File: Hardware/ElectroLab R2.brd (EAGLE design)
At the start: 175 x 100 mm, 226 parts, among them IC1 LM2902DT, IC10 CD4511BNSR, IC11 PAM8403, IC2 LM2902DT, IC3 SN74LV08ADR, IC4 SN74LV32ADR, IC5 SN74LV04ADR, IC6 4027D, IC7 4027D, IC8 NE555D, IC9 AT42QT1012, U1 USB, U2 USB-B

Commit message: Analogic accelerometer ADXL337 Layout in BRD
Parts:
- removed IR: CNY70, cny70:4
- added ACC: ADXL337, SpaceDIY_IC:LFCSP-3X3
- added C29, C30, C31: 10nF, SpaceDIY_passive_components:0603
- added C32: 100nF, SpaceDIY_passive_components:0603
- added C33, C34: 10uF, SpaceDIY_passive_components:0603
- added IC12: LM2902DT, Texas Instruments_By_element14_Batch_1:SOIC127P600X175-14N
- added R61, R63, R65: 1k, SpaceDIY_passive_components:0603
- added R62, R64, R66: 2k, SpaceDIY_passive_components:0603
- added U4: MIC5205, SparkFun:SOT23-5
- PH35: device pinhead:1X04 -> pinhead:1X03
- moved PH35 0.52 mm to (125.1, 46.7)
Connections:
- removed net A: IR.A, PH35.1
- removed net C: IR.C, PH35.3
- removed net E: IR.E, PH35.4
- removed net K: IR.K, PH35.2
- new net 3.3V: ACC.14, ACC.15, C32.1, C33.1, U4.5
- new net X: IC12.1, PH35.3, R61.1
- new net X+: ACC.5, C29.1, IC12.3
- new net X-: IC12.2, R61.2, R62.1
- new net Y: IC12.7, PH35.2, R63.1
- new net Y+: ACC.4, C30.1, IC12.5
- new net Y-: IC12.6, R63.2, R64.1
- new net Z: IC12.8, PH35.1, R65.1
- new net Z+: ACC.16, C31.1, IC12.10
- new net Z-: IC12.9, R65.2, R66.1
- net GND: now also ACC.6, ACC.7, C29.2, C30.2, C31.2, C32.2, C33.2, C34.2, IC12.11, R62.2, R64.2, R66.2, U4.2
- net VCC: now also C34.1, IC12.4, U4.1, U4.3
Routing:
- net VCC: track 395.1 -> 443.1 mm, vias 10 -> 12
- net Z: track 0.00 -> 28.8 mm, vias 0 -> 1
- net 3.3V: track 0.00 -> 22.1 mm, vias 0 -> 1
- net E: track 19.9 -> 0.00 mm
- net X+: track 0.00 -> 18.6 mm, vias 0 -> 1
- net X: track 0.00 -> 15.6 mm, vias 0 -> 1
- net Z-: track 0.00 -> 14.3 mm
- net Y: track 0.00 -> 13.5 mm
- net X-: track 0.00 -> 13.2 mm, vias 0 -> 2
- net C: track 12.5 -> 0.00 mm
- net Z+: track 0.00 -> 11.9 mm, vias 0 -> 1
- net Y+: track 0.00 -> 9.66 mm, vias 0 -> 1
- net K: track 8.81 -> 0.00 mm
- net A: track 8.78 -> 0.00 mm
- net Y-: track 0.00 -> 8.46 mm
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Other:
- board text added: "X"
- board text added: "Y"
- board text added: "Z"
- board text removed: "E"
- board text removed: "IR1"
- board text removed: "IR2"
- board text removed: "IR3"
- board text removed: "IR4"

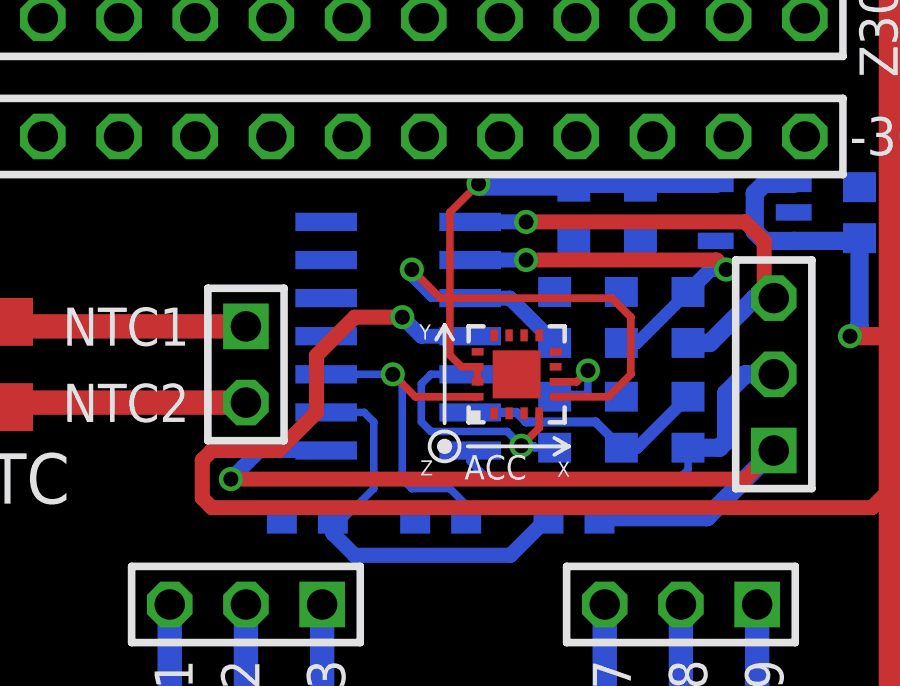
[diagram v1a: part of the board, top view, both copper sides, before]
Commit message: Minor update of ADXL337 layout
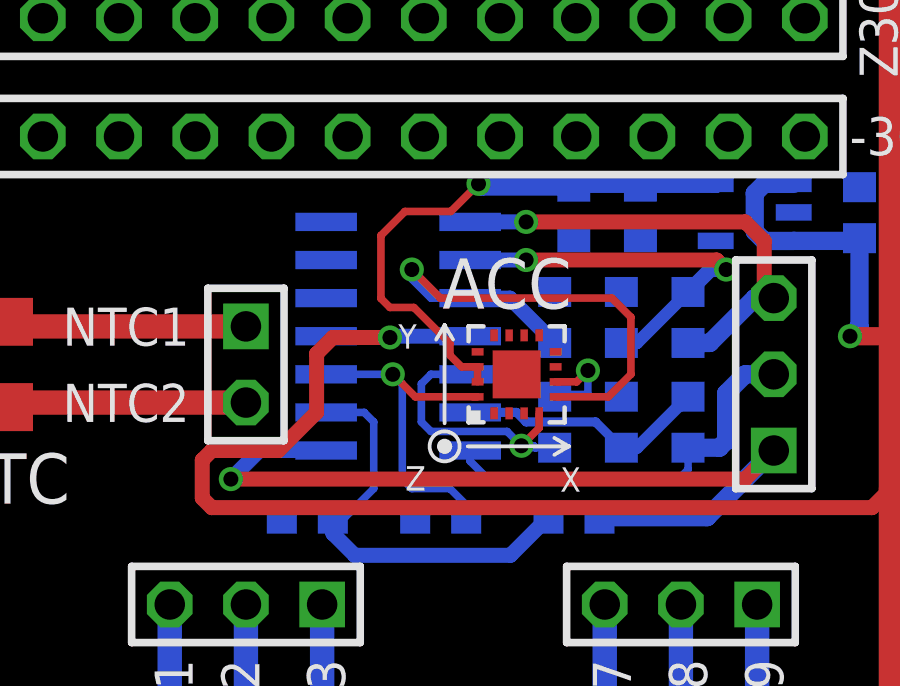
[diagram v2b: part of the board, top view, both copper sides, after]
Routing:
- net 3.3V: track 22.1 -> 25.4 mm
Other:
- board text added: "ACC"
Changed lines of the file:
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@@
 <setting verticaltext="up"/>
 </settings>
-<grid distance="0.001" unitdist="mm" unit="mm" style="lines" multiple="1" display="yes" altdistance="0.025" altunitdist="inch" altunit="inch"/>
+<grid distance="0.1" unitdist="mm" unit="mm" style="lines" multiple="1" display="yes" altdistance="0.025" altunitdist="inch" altunit="inch"/>
 <layers>
 <layer number="1" name="Top" color="4" fill="1" visible="yes" active="yes"/>
@@
 <text x="128.5875" y="61.2775" size="1.27" layer="112" rot="R90" align="center">Y30</text>
 <text x="128.5875" y="58.1025" size="1.27" layer="112" rot="R90" align="center">Z30</text>
+<text x="116.2" y="49.7" size="1.6764" layer="25" align="center">ACC</text>
 </plain>
 <attributes>
@@
 <via x="127.635" y="47.9425" extent="1-16" drill="0.5"/>
 <wire x1="127.635" y1="47.9425" x2="129" y2="47.9425" width="0.6096" layer="1"/>
-<wire x1="114.9731" y1="47.9425" x2="113.3475" y2="47.9425" width="0.5" layer="16"/>
-<wire x1="113.3475" y1="47.9425" x2="112.7125" y2="48.5775" width="0.5" layer="16"/>
-<via x="112.7125" y="48.5775" extent="1-16" drill="0.5"/>
-<wire x1="112.7125" y1="48.5775" x2="111.125" y2="48.5775" width="0.5" layer="1"/>
-<wire x1="111.125" y1="48.5775" x2="109.855" y2="47.3075" width="0.5" layer="1"/>
-<wire x1="109.855" y1="47.3075" x2="109.855" y2="45.4025" width="0.5" layer="1"/>
+<wire x1="109.855" y1="47.355" x2="109.855" y2="45.4025" width="0.5" layer="1"/>
 <wire x1="109.855" y1="45.4025" x2="108.585" y2="44.1325" width="0.5" layer="1"/>
 <wire x1="108.585" y1="44.1325" x2="106.3625" y2="44.1325" width="0.5" layer="1"/>
@@
 <wire x1="106.3625" y1="42.2275" x2="128.365" y2="42.2275" width="0.5" layer="1"/>
 <wire x1="128.365" y1="42.2275" x2="129" y2="42.8625" width="0.5" layer="1"/>
+<wire x1="109.855" y1="47.355" x2="110.4" y2="47.9" width="0.5" layer="1"/>
+<wire x1="110.4" y1="47.9" x2="111.8" y2="47.9" width="0.5" layer="1"/>
+<wire x1="114.9731" y1="47.9425" x2="112.3425" y2="47.9425" width="0.5" layer="16"/>
+<wire x1="112.3425" y1="47.9425" x2="112.3" y2="47.9" width="0.5" layer="16"/>
+<via x="112.3" y="47.9" extent="1-16" drill="0.5"/>
+<wire x1="112.3" y1="47.9" x2="111.8" y2="47.9" width="0.5" layer="1"/>
 </signal>
 <signal name="VEXT">
@@
 <wire x1="115.2225" y1="46.9215" x2="114.685" y2="46.9225" width="0.254" layer="1"/>
 <wire x1="114.685" y1="46.9225" x2="114.3" y2="47.3075" width="0.254" layer="1"/>
-<wire x1="114.3" y1="47.3075" x2="114.3" y2="52.07" width="0.254" layer="1"/>
-<wire x1="114.3" y1="52.07" x2="115.2525" y2="53.0225" width="0.254" layer="1"/>
 <via x="115.2525" y="53.0225" extent="1-16" drill="0.5"/>
 <wire x1="115.2525" y1="53.0225" x2="118.335" y2="53.0225" width="0.254" layer="16"/>
@@
 <wire x1="120.9675" y1="53.0225" x2="123.1574" y2="53.0225" width="0.6096" layer="16"/>
 <wire x1="123.1574" y1="53.0225" x2="123.1599" y2="53.02" width="0.6096" layer="16"/>
+<wire x1="114.3" y1="47.3075" x2="114.3" y2="47.7" width="0.254" layer="1"/>
+<wire x1="114.3" y1="47.7" x2="113.1" y2="48.9" width="0.254" layer="1"/>
+<wire x1="113.1" y1="48.9" x2="112.3" y2="48.9" width="0.254" layer="1"/>
+<wire x1="112.3" y1="48.9" x2="112" y2="49.2" width="0.254" layer="1"/>
+<wire x1="112" y1="49.2" x2="112" y2="51.3" width="0.254" layer="1"/>
+<wire x1="112" y1="51.3" x2="112.8" y2="52.1" width="0.254" layer="1"/>
+<wire x1="112.8" y1="52.1" x2="114.33" y2="52.1" width="0.254" layer="1"/>
+<wire x1="114.33" y1="52.1" x2="115.2525" y2="53.0225" width="0.254" layer="1"/>
 </signal>
 <signal name="X">

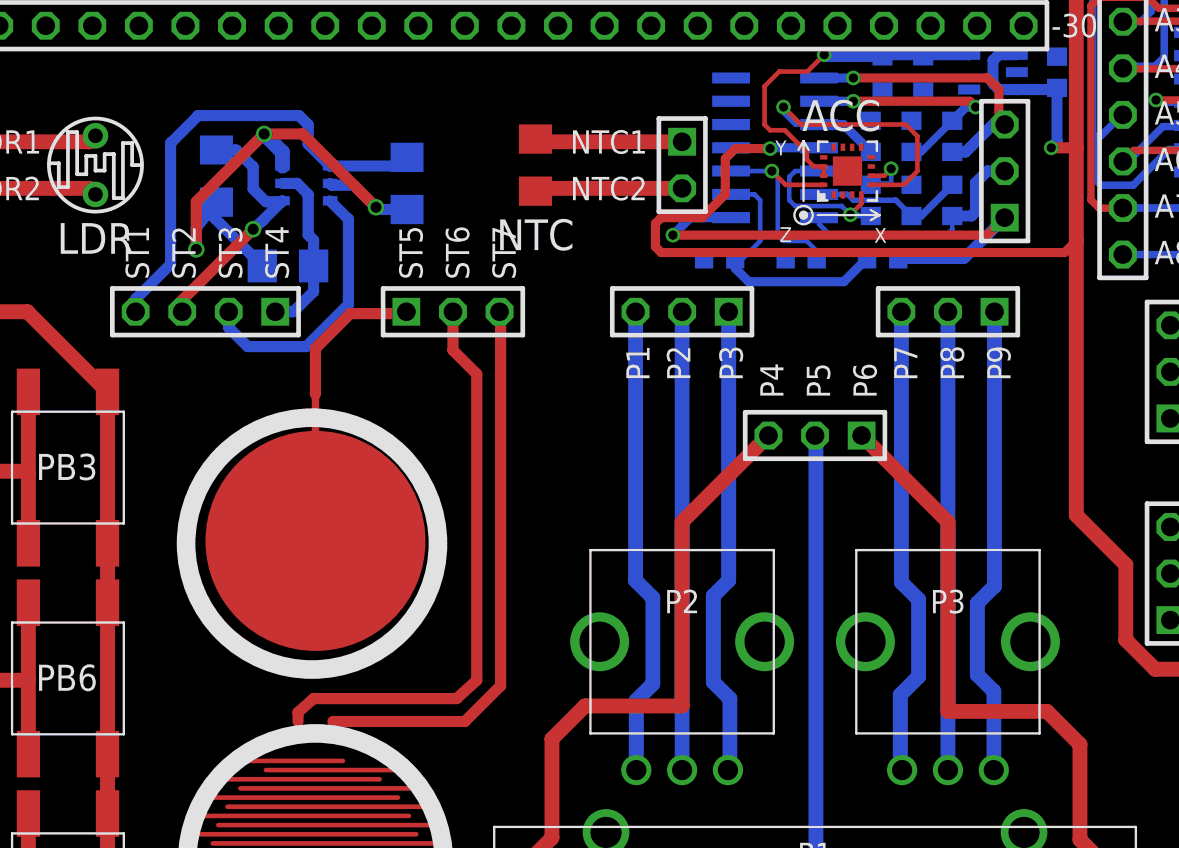
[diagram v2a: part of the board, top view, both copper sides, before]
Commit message: Modified capacitive tactile sensor. Simplified design.
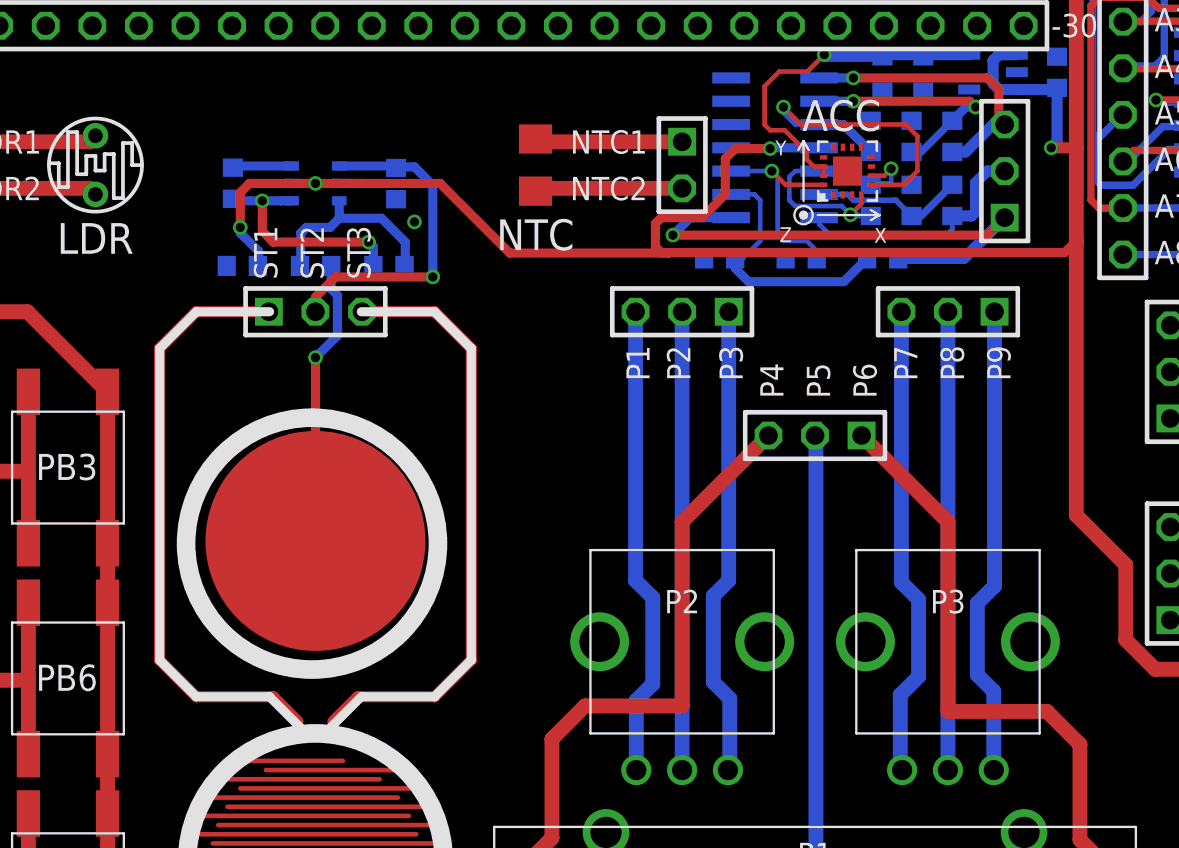
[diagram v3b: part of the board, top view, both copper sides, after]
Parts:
- removed PH34: (no value), pinhead:1X04
- added C28: 10nF, SpaceDIY_passive_components:0603
- added R67: 10k, SpaceDIY_passive_components:0603
- C22: device resistor:C1206 -> SpaceDIY_passive_components:0603
- R39, R40: device resistor:R1206 -> SpaceDIY_passive_components:0603
- moved PH21 7.50 mm to (87.5, 39.0)
- moved C22 2.50 mm to (83.5, 41.5)
- moved R40 0.98 mm to (83.0, 46.0), turned to 270 degrees
- moved R39 0.60 mm to (91.9, 46.0)
- moved IC9 0.50 mm to (87.5, 46.0)
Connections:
- removed net N$252: PH21.2, U$16.0
- removed net N$253: PH21.1, U$15.0
- removed net VCC01: C22.1, IC9.5, PH34.1
- new net N$125: PH21.1, U$16.0
- new net SENSE: R67.1, U$15.0
- net OUT01: now also PH21.2; no longer PH34.4
- net SNS: now also C28.2; no longer PH34.3
- net SNSK: now also C28.1, R67.2; no longer PH34.2
- net VCC: now also C22.1, IC9.5
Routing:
- net N$125: track 0.00 -> 32.7 mm
- net N$252: track 31.6 -> 0.00 mm
- net VCC: track 442.6 -> 473.5 mm, vias 12 -> 14
- net GND: track 92.8 -> 67.4 mm, vias 19 -> 17
- net SENSE: track 0.00 -> 9.74 mm, vias 0 -> 1
- net VCC01: track 9.62 -> 0.00 mm
- net N$253: track 8.29 -> 0.00 mm
- net OUT01: track 25.5 -> 18.2 mm, vias 0 -> 1
- net SNSK: track 14.8 -> 10.7 mm
- net N$126: track 30.4 -> 32.7 mm
- net SNS: track 13.8 -> 12.4 mm, vias 1 -> 2
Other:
- board text removed: "SNS"
- board text removed: "SNSK"
- board text removed: "ST4"
- board text removed: "ST5"
- board text removed: "ST6"
- board text removed: "ST7"
- board text removed: "VCC"

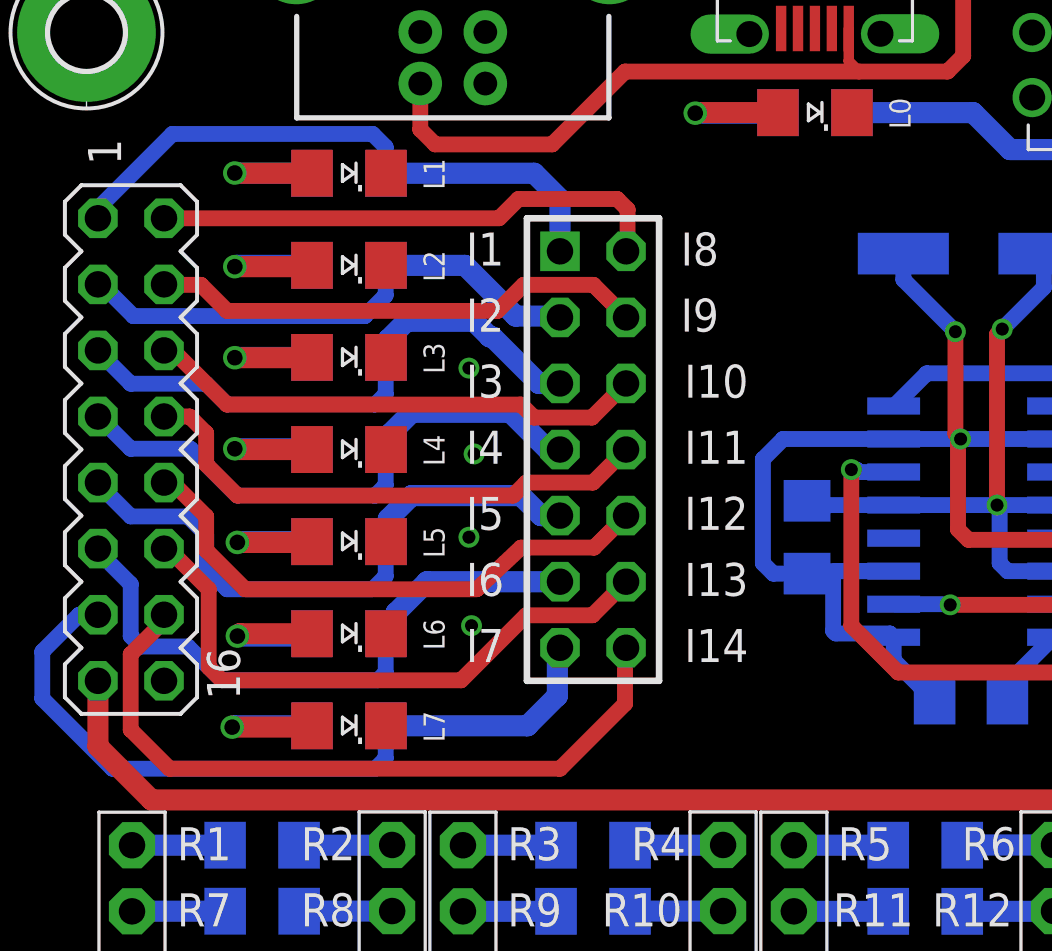
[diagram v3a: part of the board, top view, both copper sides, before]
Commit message: Mod: Seriegraphy and layout of ArduLab interface. Modified CTI related seriegraphy
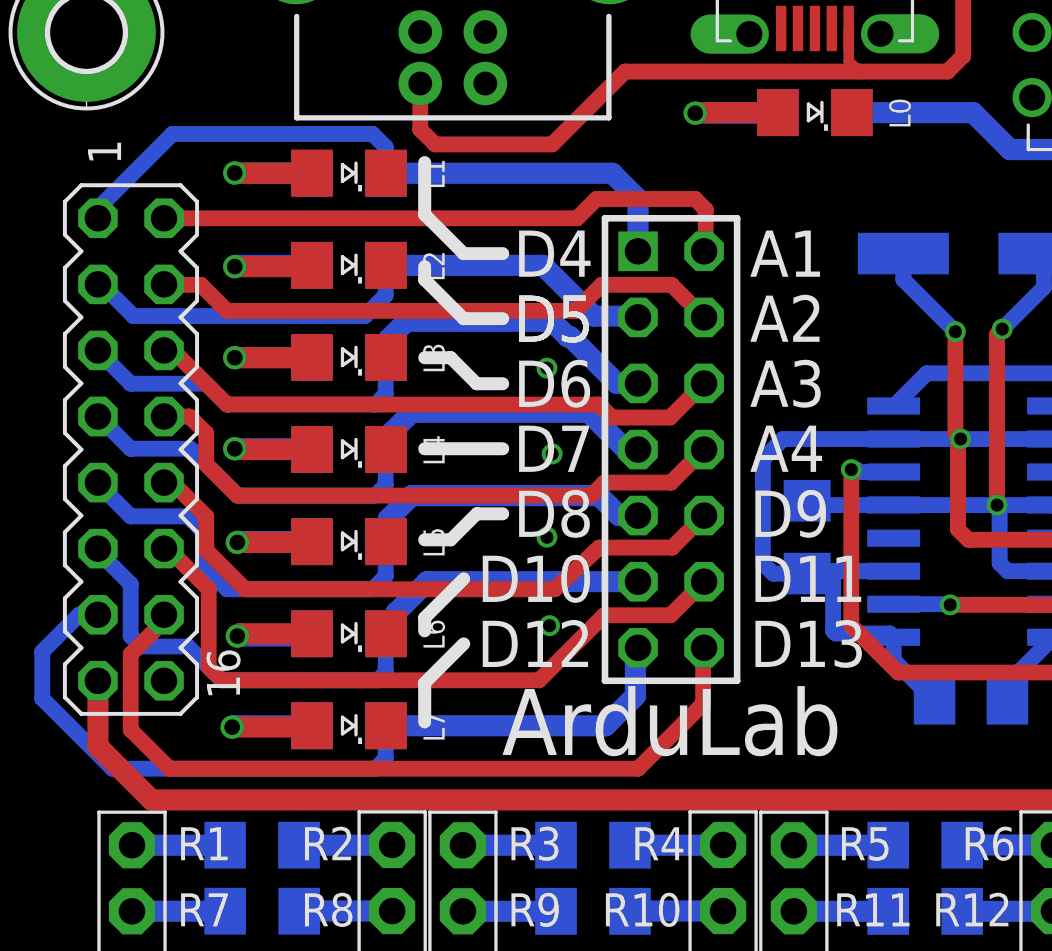
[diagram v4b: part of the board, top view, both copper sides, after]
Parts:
- moved PH41 3.00 mm to (27.5, 79.0)
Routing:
- net D9: track 21.4 -> 24.4 mm
- net D8: track 23.3 -> 26.3 mm
- net D6: track 22.0 -> 25.0 mm
- net D5: track 19.4 -> 22.4 mm
- net D4: track 22.1 -> 25.1 mm
- net D3: track 19.1 -> 22.1 mm
- net D2: track 20.6 -> 23.6 mm
- net D13: track 27.8 -> 30.8 mm
- net D12: track 29.2 -> 32.2 mm
- net D11: track 23.2 -> 26.2 mm
- net D10: track 23.8 -> 26.8 mm
- net D7: track 20.5 -> 23.5 mm
- net D1: track 19.9 -> 22.9 mm
- net D0: track 23.0 -> 26.0 mm
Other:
- board text added: "ArduLab"
- board text added: "D10"
- board text added: "D11"
- board text added: "D12"
- board text added: "D13"
- board text added: "D9"
- board text removed: "I1"
- board text removed: "I10"
- board text removed: "I11"
- board text removed: "I12"
- board text removed: "I13"
- board text removed: "I14"
- board text removed: "I2"
- board text removed: "I3"
- board text removed: "I4"
- board text removed: "I5"
- board text removed: "I6"
- board text removed: "I7"
- board text removed: "I8"
- board text removed: "I9"
